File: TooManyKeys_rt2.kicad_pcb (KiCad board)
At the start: 6 copper layers, 156 x 116.5 mm, 89 parts, among them U1 TLV61070ADBV, U2 SN74LV1T126DBVR

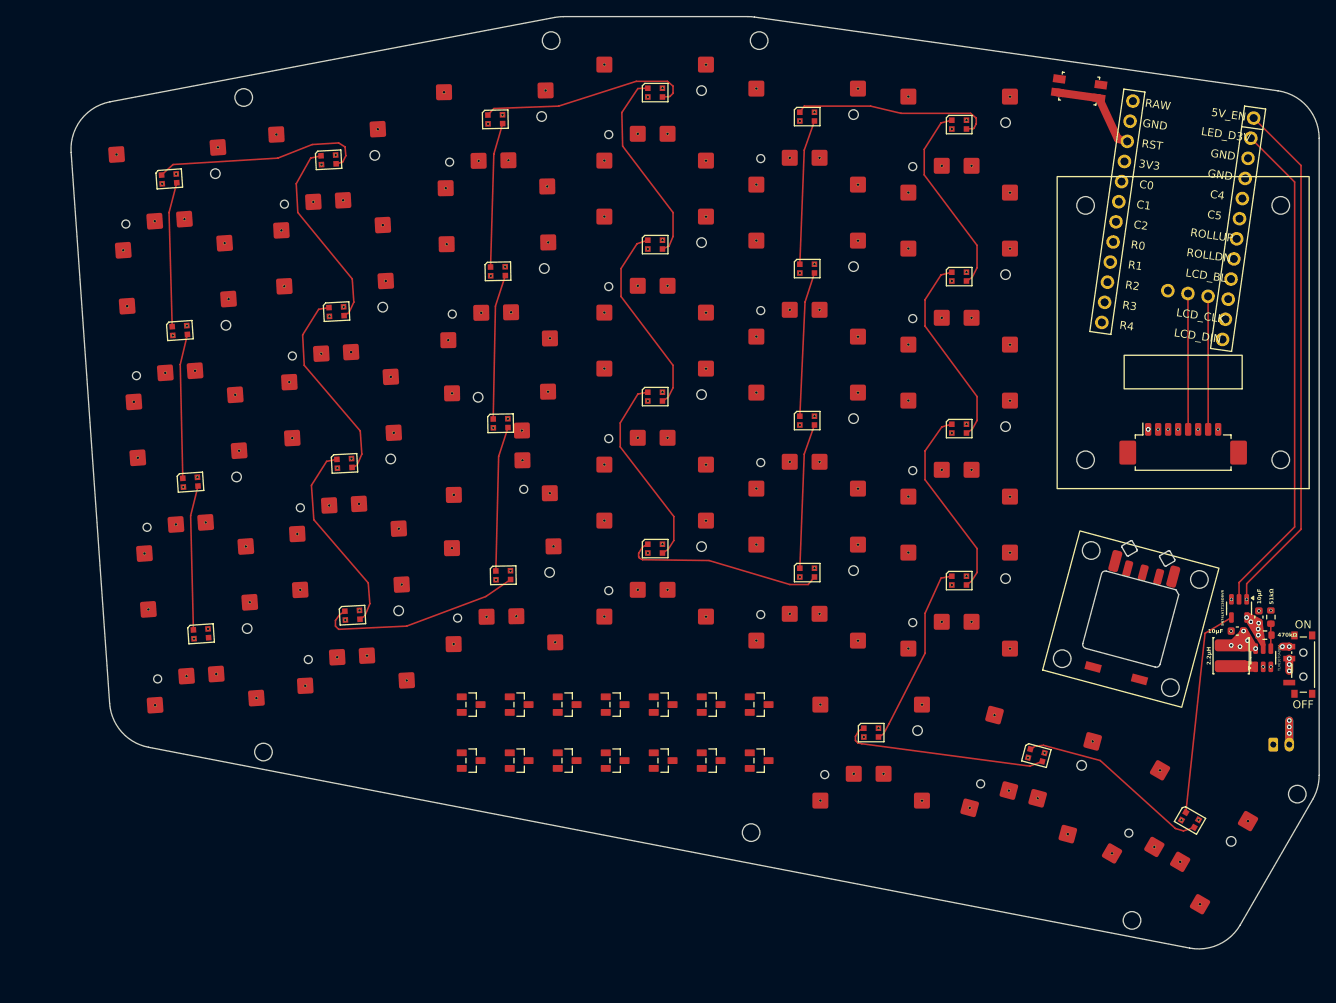
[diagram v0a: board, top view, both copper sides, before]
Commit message: Finish clean routing. Attempted sync of schematic failed, but board LGTM and passes DRC other than CKW12 edge issues of no concern.
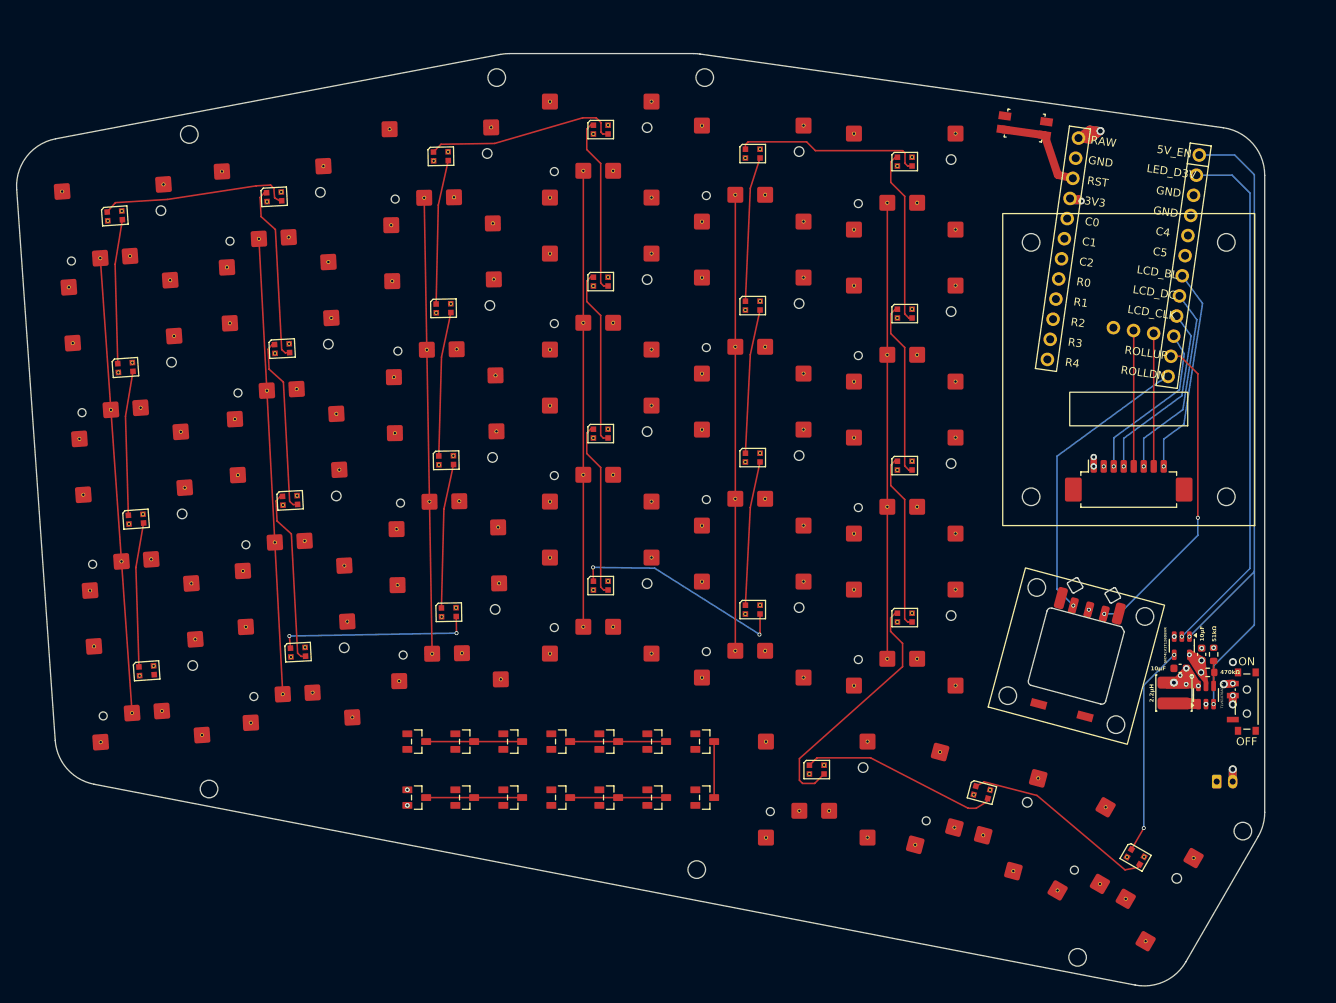
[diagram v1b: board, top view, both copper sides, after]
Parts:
- moved R1 8.54 mm to (186.3, 162.4)
- moved L1 8.54 mm to (182.1, 165.0)
- moved U2 8.54 mm to (183.1, 159.0)
- moved C2 8.54 mm to (185.6, 160.1)
- moved C1 8.54 mm to (182.9, 161.9)
- moved U1 8.54 mm to (186.1, 165.2)
- moved R2 8.54 mm to (187.1, 160.1)
- moved JST1 8.45 mm to (188.5, 176.0)
- moved PWR1 8.44 mm to (191.2, 166.0)
- moved S15 8.23 mm to (110.5, 116.0)
- moved LED3 8.23 mm to (51.0, 124.3)
- moved LED19 8.23 mm to (129.5, 116.5)
- moved S19 8.23 mm to (129.5, 119.0)
- moved D8 8.23 mm to (93.5, 171.0)
- moved RE1 8.23 mm to (169.9, 160.3)
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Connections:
- D12 pad 1: finger_inner_bottom -> finger_index_bottom
- D12 pad 2: finger_index_bottom -> finger_inner_bottom
- D2 pad 1: finger_middle_num -> finger_ring_num
- D2 pad 2: finger_ring_num -> finger_middle_num
- D3 pad 1: finger_inner_num -> finger_index_num
- D3 pad 2: finger_index_num -> finger_inner_num
- D5 pad 1: finger_middle_top -> finger_ring_top
- D5 pad 2: finger_ring_top -> finger_middle_top
- D6 pad 1: finger_inner_top -> finger_index_top
- D6 pad 2: finger_index_top -> finger_inner_top
- D8 pad 1: finger_middle_home -> finger_ring_home
- D8 pad 2: finger_ring_home -> finger_middle_home
- D9 pad 1: finger_inner_home -> finger_index_home
- D9 pad 2: finger_index_home -> finger_inner_home
- MCU1 pad 10: LCD_DC -> LCD_DIN
- MCU1 pad 11: LCD_CLK -> ROLLUP
- MCU1 pad 12: LCD_DIN -> ROLLDN
- MCU1 pad 7: ROLLUP -> LCD_BL
- MCU1 pad 8: ROLLDN -> LCD_DC
- MCU1 pad 9: LCD_BL -> LCD_CLK
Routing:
- net RAW: track 108.8 -> 264.4 mm, vias 7 -> 10
- net C2: track 0.00 -> 57.0 mm
- net C3: track 0.00 -> 57.0 mm
- net C0: track 0.00 -> 57.0 mm
- net C4: track 0.00 -> 57.0 mm
- net C5: track 0.00 -> 57.0 mm
- net C1: track 0.00 -> 57.0 mm
- net 3V3: track 35.2 -> 79.8 mm, vias 1 -> 3
- net ROLLUP: track 0.00 -> 40.2 mm, vias 0 -> 2
- net ROLLDN: track 0.00 -> 36.6 mm, vias 0 -> 1
- net 5V_EN: track 75.5 -> 87.7 mm
- net R0: track 0.00 -> 12.0 mm
- net R1: track 0.00 -> 12.0 mm
- net R2: track 0.00 -> 12.0 mm
- net R3: track 0.00 -> 12.0 mm
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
